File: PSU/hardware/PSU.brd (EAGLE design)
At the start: 143.5 x 58.5 mm, 209 parts, among them J1 SWD, J2 UART, Q1 PMOS-DPAK, Q10 PMOS-SOT23, Q11 NPN, Q12 PMOS-SOT23, Q13 NPN, Q14 NPN, Q2 PMOS-SOT23, Q3 NPN, Q4 PMOS-SOT23, Q5 NMOS-SOT23, Q6 PMOS-DPAK, Q7 PMOS-SOT23, Q8 NMOS-SOT23, Q9 PMOS-DPAK, U1 LM2576, U10 4069, U11 LTV-247, U12 74HC08, U13 STM8S003K3T6C, U14 74HC08, U15 4051, U16 358, U17 358, U18 74HC32, U2 MT3608, U3 7805, U4 324, U5 MC34063, U6 MT3608, U7 LM2576, U8 MC34063, U9 TP4056

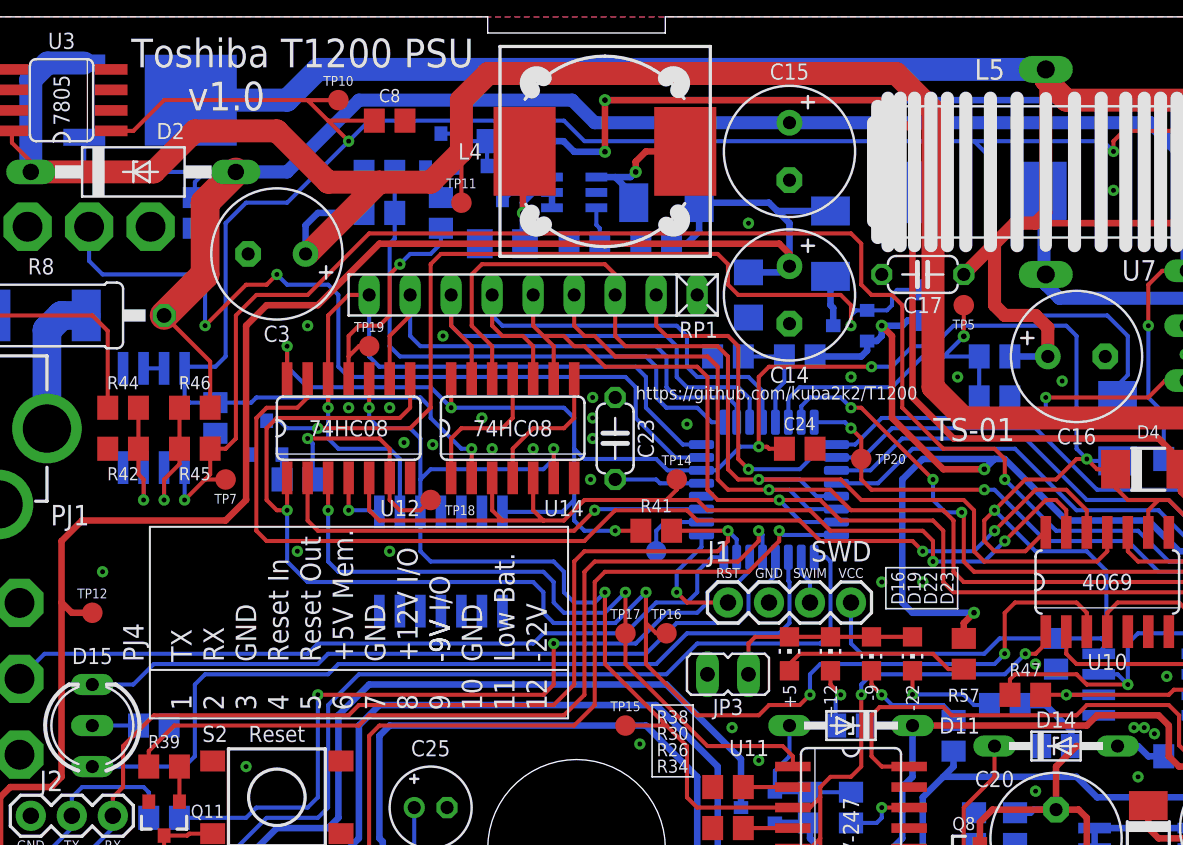
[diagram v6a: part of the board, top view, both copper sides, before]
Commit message: [HW/PSU] Fix open-drain GPIO usage
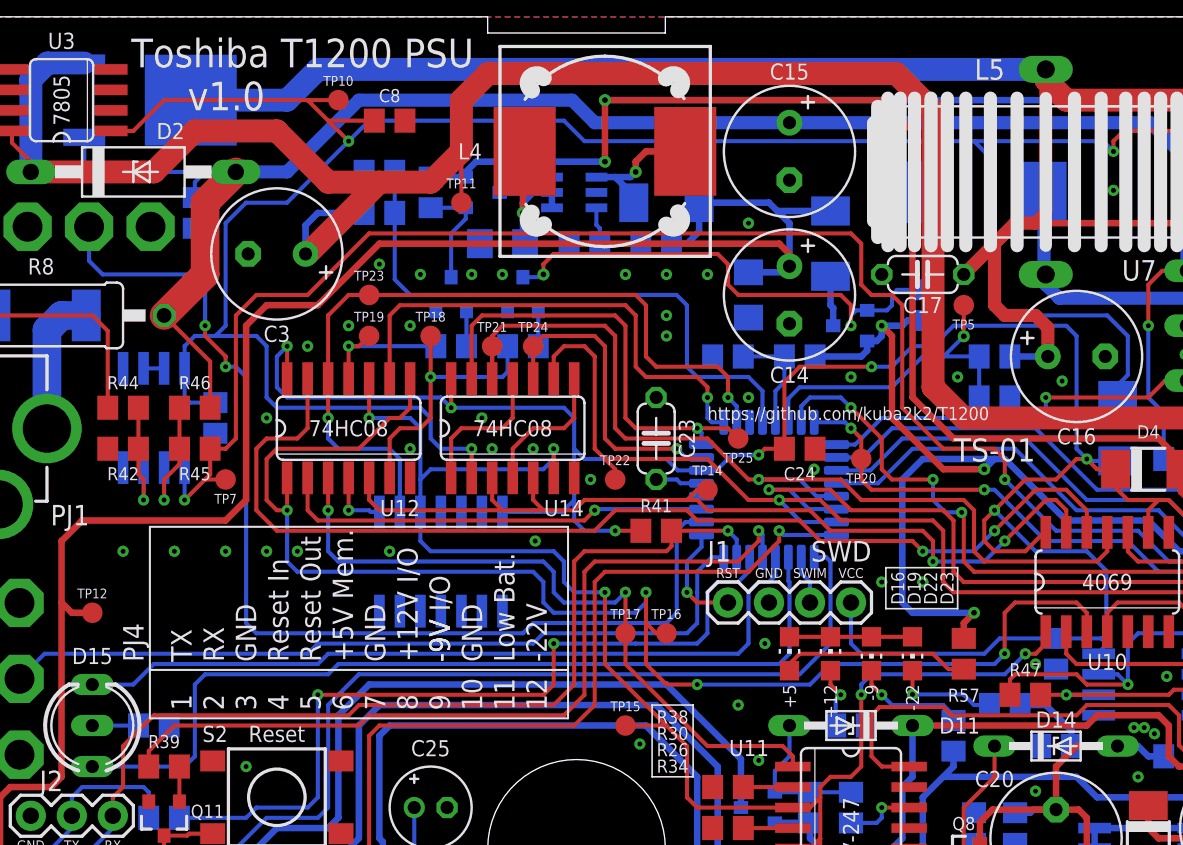
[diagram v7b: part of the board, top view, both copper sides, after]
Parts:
- removed JP3: LedVReg, jumper:JP1
- removed RP1: 8x10k, custom:RN-9
- removed TP13: TPB1,27, testpad:B1,27
- added TP21, TP22, TP23, TP24, TP25: TPB1,27, testpad:B1,27
- moved Q14 18.2 mm to (43.2, 41.3)
- moved R80 16.2 mm to (43.2, 38.1), turned to 180 degrees
- moved TP18 10.2 mm to (37.5, 38.7)
- moved Q13 8.91 mm to (38.7, 41.3)
- moved R78 8.28 mm to (38.7, 38.1), turned to 180 degrees
- moved R77 5.46 mm to (37.5, 47.6), turned to 90 degrees
- moved C23 2.54 mm to (51.4, 32.4)
- moved TP14 2.01 mm to (54.6, 29.2)
- moved Q12 1.42 mm to (40.6, 47.6), turned to 90 degrees
- moved TP19 0.63 mm to (33.7, 38.7)
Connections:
- removed net LED1_EN: D16.C, D19.C, D22.A, D23.A, JP3.1
- removed net PA1: TP13.TP, U13.2
- net CHG_B_CTRL: no longer RP1.4
- net GND: now also D16.C, D19.C, D22.A, D23.A; no longer JP3.2, RP1.1
- net HDD5_CTRL: now also U13.9; no longer RP1.8, U13.10
- net MAIN_CTRL: now also TP24.TP, U13.7; no longer RP1.6, U13.12
- net MEM_CTRL: now also TP23.TP, U13.10; no longer RP1.9, U13.8
- net PRI_CTRL: now also TP21.TP; no longer RP1.3
- net PRI_OK_CTRL: now also TP25.TP, U13.8; no longer RP1.7, U13.11
- net SEC_CTRL: now also TP22.TP; no longer RP1.5
- net V+SENSE: now also U13.12; no longer U13.9
- net ^CHG_CTRL: no longer RP1.2
- net ^HDDON: now also U13.2; no longer U13.7
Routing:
- net +5VMEM_G: track 55.5 -> 30.7 mm
- net CHG_B_CTRL: track 134.9 -> 112.7 mm
- net ^CHG_CTRL: track 45.6 -> 23.7 mm, vias 2 -> 1
- net ^HDDON: track 52.9 -> 66.6 mm
- net LED1_EN: track 12.2 -> 0.00 mm
- net MAIN_CTRL: track 30.0 -> 19.2 mm, vias 0 -> 1
- net PRI_CTRL: track 68.7 -> 60.6 mm
- net GND: track 0.00 -> 7.62 mm, vias 95 -> 106
- net MEM_BACKUP: track 14.7 -> 8.94 mm
- net VBACKUP: track 173.3 -> 178.1 mm
- net PA1: track 4.30 -> 0.00 mm
- net SEC_CTRL: track 94.2 -> 90.0 mm
- net HDD5_EN: track 88.9 -> 85.3 mm
- net VCCINT: track 225.3 -> 228.7 mm
- net RX: track 63.9 -> 60.6 mm
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
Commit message: [HW/PSU] Fix backup charger enabling, remove standby LEDs
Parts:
- removed D18, D20: GREEN, led:CHIP-LED0805
- added Q15: PMOS-SOT23, SparkFun-DiscreteSemi:SOT23-3
- added R81: 10k, rcl:R0805
- moved D17 1.27 mm to (118.0, 43.2), turned to 90 degrees
- moved D21 1.27 mm to (109.0, 38.7), turned to 90 degrees
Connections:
- removed net CHG_B_STBY: D20.C, U9.6
- new net CHG_B_SW: Q15.3, R31.1, R32.1, U9.8
- net +5V: now also Q15.2, R81.2; no longer R31.1, R32.1
- net CHG_B_CTRL: now also Q15.1; no longer U9.8
- net CHG_B_STATE: now also R81.1
- net LED2_EN: no longer D20.A
- net LED3_EN: no longer D18.C
- net VCCINT: no longer D18.A
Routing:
- net CHG_B_SW: track 0.00 -> 17.7 mm, vias 0 -> 1
- net CHG_B_STBY: track 16.4 -> 0.00 mm, vias 1 -> 0
- net CHG_B_CTRL: track 112.7 -> 103.4 mm
- net +5V: track 190.5 -> 187.7 mm
- net VCCINT: track 228.7 -> 226.8 mm
- net LED3_EN: track 9.81 -> 8.23 mm
- net LED2_EN: track 13.4 -> 12.5 mm, vias 1 -> 0
- net GND: vias 106 -> 105
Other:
- board text removed: "Full"
